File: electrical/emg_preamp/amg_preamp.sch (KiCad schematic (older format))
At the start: 26 parts, among them J1 in, J2 T1, J3 T2, J4 Conn_01x05, U1 TSZ124IPT

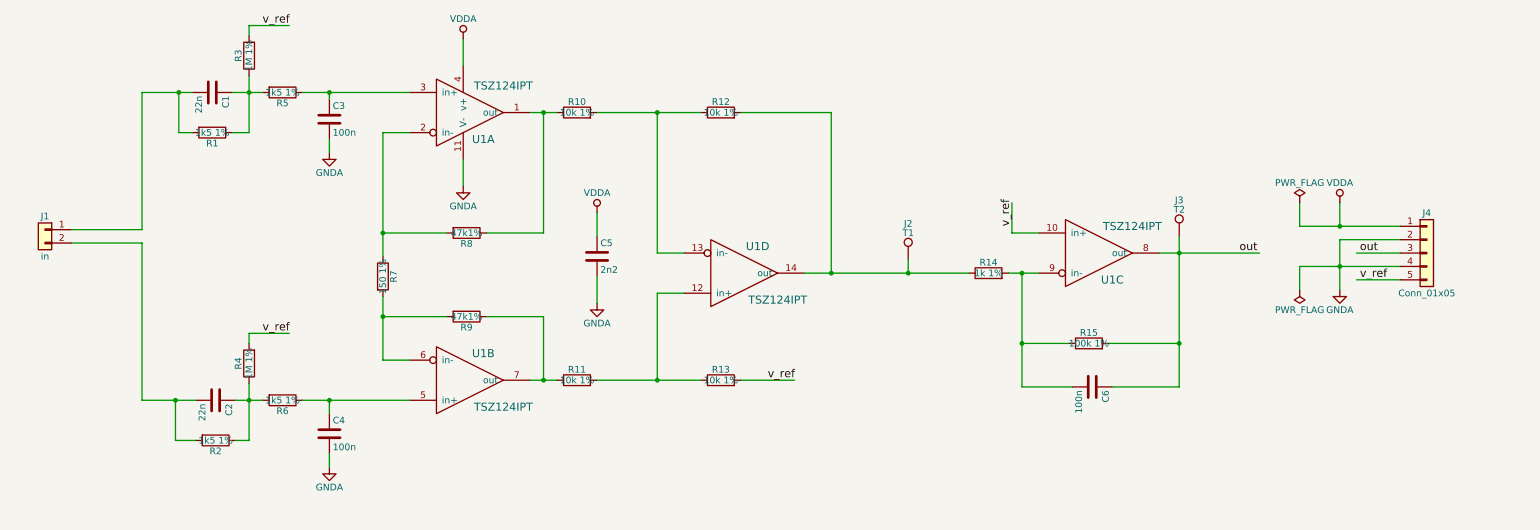
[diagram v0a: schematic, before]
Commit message: Added output resistance to preamp board.
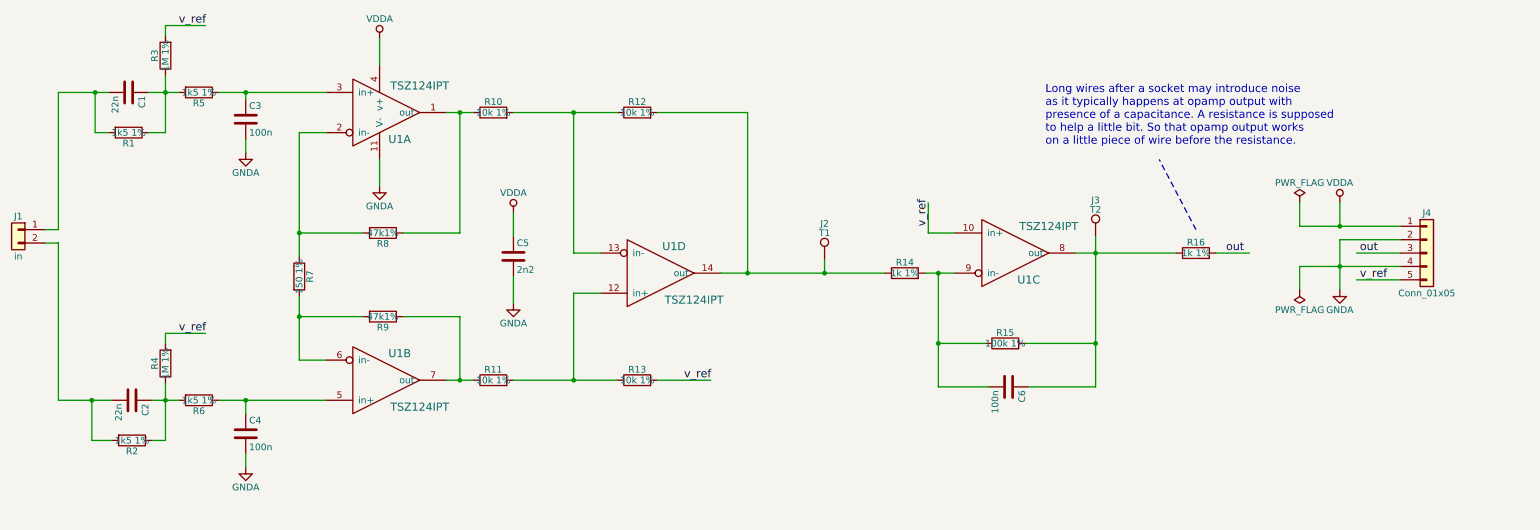
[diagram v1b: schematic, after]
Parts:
- added R16: 1k 1%, Resistor_SMD:R_0603_1608Metric, symbol R
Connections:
- wire segments 72 -> 73
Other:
- note added: "Long wires after a socket may introduce noise \nas it typically happens at opamp output with \npresence of a capacitance. A resistance is supposed \nto help a little bit. So that opamp output works \non a little piece of wire before the resistance."
- moved on the sheet: C1, C2, C3, C4, C5, C6, J1, J2, J3, R1, R10, R11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

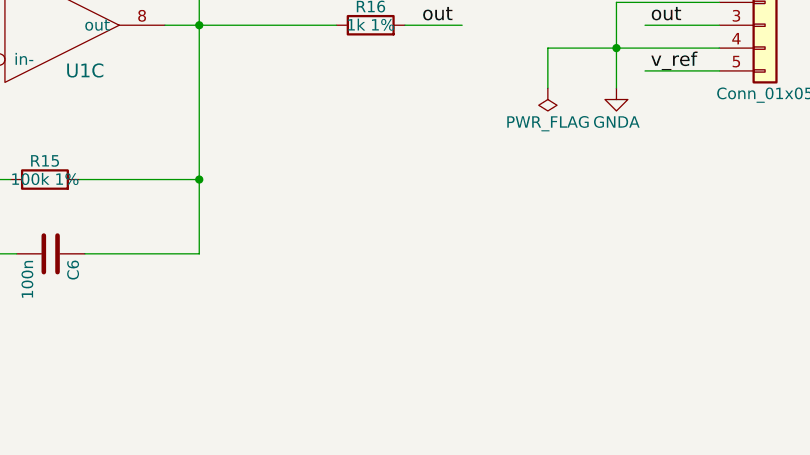
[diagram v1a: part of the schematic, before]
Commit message: Added filtering bypass caps.
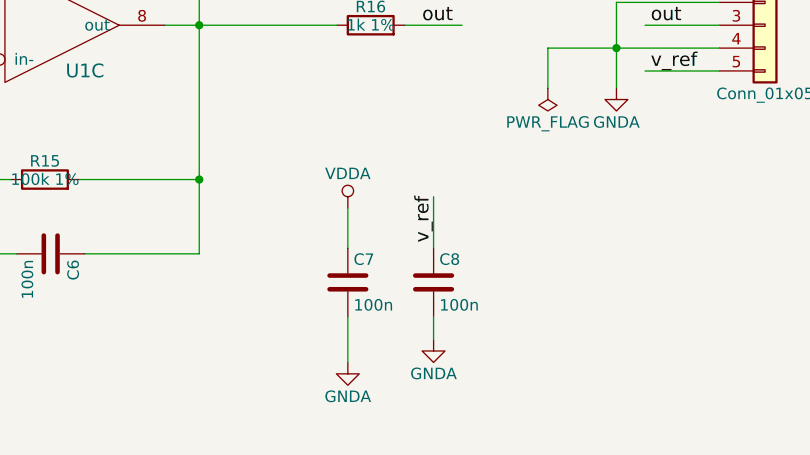
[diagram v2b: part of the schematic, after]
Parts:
- added C7, C8: 100n, Capacitor_SMD:C_0603_1608Metric, symbol C
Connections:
- wire segments 73 -> 77
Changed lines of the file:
@@
 $EndComp
 $Comp
-L VDDA #PWR01
+L VDDA #PWR3
 U 1 1 5BA0610D
 P 3225 2150
-F 0 "#PWR01" H 3225 2000 50  0001 C CNN
+F 0 "#PWR3" H 3225 2000 50  0001 C CNN
 F 1 "VDDA" H 3225 2300 50  0000 C CNN
 F 2 "" H 3225 2150 50  0001 C CNN
@@
 $EndComp
 $Comp
-L GNDA #PWR02
+L GNDA #PWR4
 U 1 1 5BA0610E
 P 3225 3250
-F 0 "#PWR02" H 3225 3000 50  0001 C CNN
+F 0 "#PWR4" H 3225 3000 50  0001 C CNN
 F 1 "GNDA" H 3225 3100 50  0000 C CNN
 F 2 "" H 3225 3250 50  0001 C CNN
@@
 $EndComp
 $Comp
-L VDDA #PWR03
+L VDDA #PWR5
 U 1 1 5BA0610F
 P 4225 3450
-F 0 "#PWR03" H 4225 3300 50  0001 C CNN
+F 0 "#PWR5" H 4225 3300 50  0001 C CNN
 F 1 "VDDA" H 4225 3600 50  0000 C CNN
 F 2 "" H 4225 3450 50  0001 C CNN
@@
 $EndComp
 $Comp
-L GNDA #PWR04
+L GNDA #PWR6
 U 1 1 5BA06110
 P 4225 4125
-F 0 "#PWR04" H 4225 3875 50  0001 C CNN
+F 0 "#PWR6" H 4225 3875 50  0001 C CNN
 F 1 "GNDA" H 4225 3975 50  0000 C CNN
 F 2 "" H 4225 4125 50  0001 C CNN
@@
 $EndComp
 $Comp
-L GNDA #PWR05
+L GNDA #PWR1
 U 1 1 5BA0611F
 P 2225 3000
-F 0 "#PWR05" H 2225 2750 50  0001 C CNN
+F 0 "#PWR1" H 2225 2750 50  0001 C CNN
 F 1 "GNDA" H 2225 2850 50  0000 C CNN
 F 2 "" H 2225 3000 50  0001 C CNN
@@
 $EndComp
 $Comp
-L GNDA #PWR06
+L GNDA #PWR2
 U 1 1 5BA06121
 P 2225 5350
-F 0 "#PWR06" H 2225 5100 50  0001 C CNN
+F 0 "#PWR2" H 2225 5100 50  0001 C CNN
 F 1 "GNDA" H 2225 5200 50  0000 C CNN
 F 2 "" H 2225 5350 50  0001 C CNN
@@
 Connection ~ 10400 3850
 $Comp
-L GNDA #PWR07
+L GNDA #PWR11
 U 1 1 5BA093C6
 P 10400 4025
-F 0 "#PWR07" H 10400 3775 50  0001 C CNN
+F 0 "#PWR11" H 10400 3775 50  0001 C CNN
 F 1 "GNDA" H 10400 3875 50  0000 C CNN
 F 2 "" H 10400 4025 50  0001 C CNN
@@
 	10400 3550 10400 3375
 $Comp
-L VDDA #PWR08
+L VDDA #PWR10
 U 1 1 5BA09791
 P 10400 3375
-F 0 "#PWR08" H 10400 3225 50  0001 C CNN
+F 0 "#PWR10" H 10400 3225 50  0001 C CNN
 F 1 "VDDA" H 10400 3525 50  0000 C CNN
 F 2 "" H 10400 3375 50  0001 C CNN
@@
 $EndComp
 $Comp
-L PWR_FLAG #FLG09
+L PWR_FLAG #FLG1
 U 1 1 5BA09CBD
 P 10100 3375
-F 0 "#FLG09" H 10100 3450 50  0001 C CNN
+F 0 "#FLG1" H 10100 3450 50  0001 C CNN
 F 1 "PWR_FLAG" H 10100 3525 50  0000 C CNN
 F 2 "" H 10100 3375 50  0001 C CNN
@@
 	10100 3850 10100 4025
 $Comp
-L PWR_FLAG #FLG010
+L PWR_FLAG #FLG2
 U 1 1 5BA0A475
 P 10100 4025
-F 0 "#FLG010" H 10100 4100 50  0001 C CNN
+F 0 "#FLG2" H 10100 4100 50  0001 C CNN
 F 1 "PWR_FLAG" H 10100 4175 50  0000 C CNN
 F 2 "" H 10100 4025 50  0001 C CNN
@@
 Text Notes 8200 2950 0    60   ~ 0
 Long wires after a socket may introduce noise \nas it typically happens at opamp output with \npresence of a capacitance. A resistance is supposed \nto help a little bit. So that opamp output works \non a little piece of wire before the resistance.
+$Comp
+L C C8
+U 1 1 5BA2AEB9
+P 9600 4875
+F 0 "C8" H 9625 4975 50  0000 L CNN
+F 1 "100n" H 9625 4775 50  0000 L CNN
+F 2 "Capacitor_SMD:C_0603_1608Metric" H 9638 4725 50  0001 C CNN
+F 3 "" H 9600 4875 50  0001 C CNN
+	1    9600 4875
+	1    0    0    -1
+$EndComp
+Wire Wire Line
+	9600 4500 9600 4725
+Text Label 9600 4700 1    60   ~ 0
+v_ref
+Wire Wire Line
+	9600 5025 9600 5125
+$Comp
+L GNDA #PWR9
+U 1 1 5BA2B5DD
+P 9600 5125
+F 0 "#PWR9" H 9600 4875 50  0001 C CNN
+F 1 "GNDA" H 9600 4975 50  0000 C CNN
+F 2 "" H 9600 5125 50  0001 C CNN
+F 3 "" H 9600 5125 50  0001 C CNN
+	1    9600 5125
+	1    0    0    -1
+$EndComp
+$Comp
+L C C7
+U 1 1 5BA2C11E
+P 9225 4875
+F 0 "C7" H 9250 4975 50  0000 L CNN
+F 1 "100n" H 9250 4775 50  0000 L CNN
+F 2 "Capacitor_SMD:C_0603_1608Metric" H 9263 4725 50  0001 C CNN
+F 3 "" H 9225 4875 50  0001 C CNN
+	1    9225 4875
+	1    0    0    -1
+$EndComp
+$Comp
+L VDDA #PWR7
+U 1 1 5BA2C124
+P 9225 4550
+F 0 "#PWR7" H 9225 4400 50  0001 C CNN
+F 1 "VDDA" H 9225 4700 50  0000 C CNN
+F 2 "" H 9225 4550 50  0001 C CNN
+F 3 "" H 9225 4550 50  0001 C CNN
+	1    9225 4550
+	1    0    0    -1
+$EndComp
+$Comp
+L GNDA #PWR8
+U 1 1 5BA2C12A
+P 9225 5225
+F 0 "#PWR8" H 9225 4975 50  0001 C CNN
+F 1 "GNDA" H 9225 5075 50  0000 C CNN
+F 2 "" H 9225 5225 50  0001 C CNN
+F 3 "" H 9225 5225 50  0001 C CNN
+	1    9225 5225
+	1    0    0    -1
+$EndComp
+Wire Wire Line
+	9225 4725 9225 4550
+Wire Wire Line
+	9225 5225 9225 5025
 $EndSCHEMATC

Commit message: Documented changes.
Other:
- note added: "100 Ohm in series \nwith 4u7\n"
- note added: "2 x 4u7 in \nparallel"
- note added: "2n2"
- note added: "3kOhm"
- note added: "Take Vref from a different board \nthrough 100 Ohm resistor."
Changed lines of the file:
@@
 Wire Wire Line
 	9225 5225 9225 5025
+Wire Notes Line
+	2550 3925 1850 3600
+Text Notes 1675 3575 0    60   ~ 0
+3kOhm
+Wire Notes Line
+	7125 4025 6525 5025
+Text Notes 6225 5250 0    60   ~ 0
+100 Ohm in series \nwith 4u7\n
+Wire Notes Line
+	7950 5000 7700 5625
+Text Notes 7625 5725 0    60   ~ 0
+2n2
+Text Notes 9300 3475 0    60   ~ 0
+2 x 4u7 in \nparallel
+Wire Notes Line
+	10725 4050 10700 4850
+Text Notes 9975 5050 0    60   ~ 0
+Take Vref from a different board \nthrough 100 Ohm resistor.
 $EndSCHEMATC
